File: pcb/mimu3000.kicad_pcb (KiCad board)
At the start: 2 copper layers, 54.9 x 25.9 mm, 13 parts, among them SW1 ONOFF, U1 AQY211EH, U2 ATTINY48U

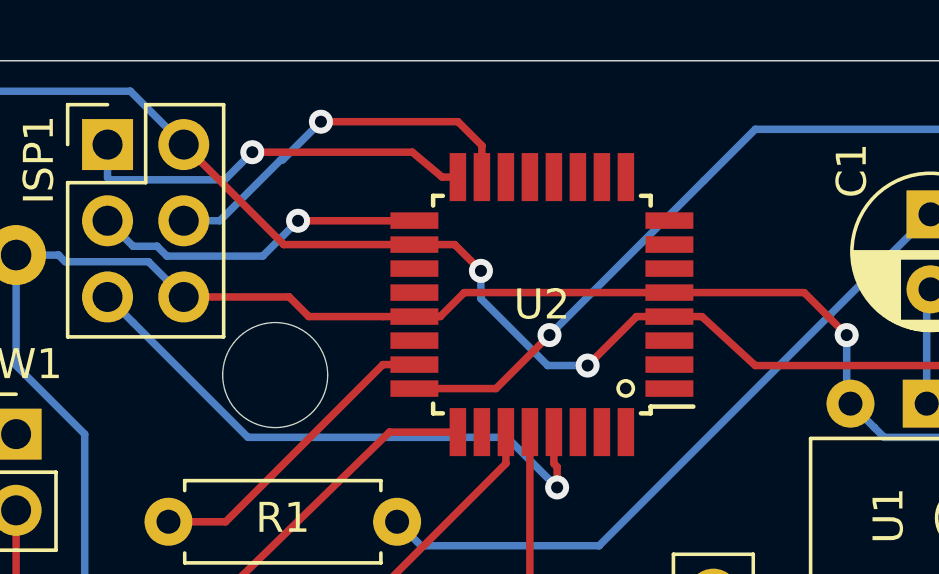
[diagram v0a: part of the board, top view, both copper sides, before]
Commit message: Still too much progmem
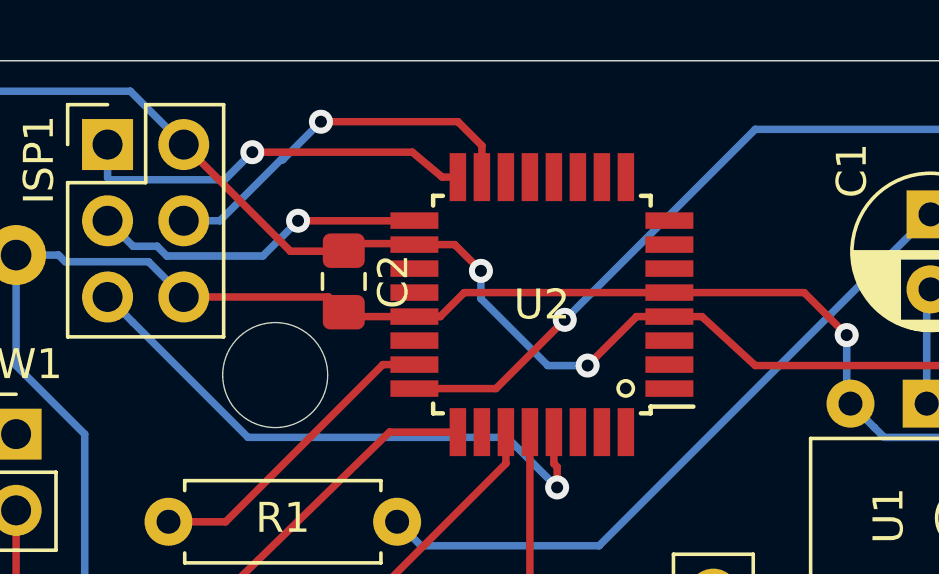
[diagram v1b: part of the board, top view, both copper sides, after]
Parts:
- added C2: 0.1uF, Capacitor_SMD:C_0805_2012Metric_Pad1.15x1.40mm_HandSolder, F.Cu at (178.6, 108.2)
- renumbered BT to BT1
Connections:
- U2 pad 1: Net-(U2-Pad1) -> (no net)
- U2 pad 10: Net-(U2-Pad10) -> (no net)
- U2 pad 11: Net-(U2-Pad11) -> (no net)
- U2 pad 12: Net-(U2-Pad12) -> (no net)
- U2 pad 13: Net-(U2-Pad13) -> (no net)
- U2 pad 14: Net-(U2-Pad14) -> (no net)
- U2 pad 19: Net-(U2-Pad19) -> (no net)
- U2 pad 2: Net-(U2-Pad2) -> (no net)
- U2 pad 20: Net-(U2-Pad20) -> (no net)
- U2 pad 22: Net-(U2-Pad22) -> (no net)
- U2 pad 26: Net-(U2-Pad26) -> (no net)
- U2 pad 3: Net-(U2-Pad3) -> (no net)
- U2 pad 30: Net-(U2-Pad30) -> (no net)
- U2 pad 31: Net-(U2-Pad31) -> (no net)
- U2 pad 32: Net-(U2-Pad32) -> (no net)
- U2 pad 6: Net-(U2-Pad6) -> (no net)
- U2 pad 7: Net-(U2-Pad7) -> (no net)
- U2 pad 8: Net-(U2-Pad8) -> (no net)
- U2 pad 9: Net-(U2-Pad9) -> (no net)

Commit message: We have to use Attiny88
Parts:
- added C3: 0.1uF, Capacitor_SMD:C_0805_2012Metric_Pad1.15x1.40mm_HandSolder, F.Cu at (186.7, 103.4)
- U2: value ATTINY48U -> ATTINY88AU; footprint Housings_QFP:TQFP-32_7x7mm_Pitch0.8mm -> Package_DFN_QFN:QFN-32-1EP_5x5mm_P0.5mm_EP3.1x3.1mm
- moved C2 12.7 mm to (191.3, 108.5), turned to 90 degrees
- moved U2 1.48 mm to (185.9, 107.7)
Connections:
- U2 pad 18: +3V0 -> Net-(C3-Pad1)
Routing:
- net +3V0: track 91.3 -> 102.8 mm
- net Net-(C3-Pad1): track 0.00 -> 9.23 mm, vias 0 -> 2
- net LED: track 12.6 -> 16.5 mm
- net Net-(SENS1-Pad4): track 14.4 -> 17.9 mm
- net Net-(SENS1-Pad3): track 21.6 -> 25.0 mm
- net MUTE: track 10.4 -> 13.4 mm
- net Net-(ISP1-Pad3): track 11.4 -> 13.9 mm
- net GND: track 140.4 -> 138.1 mm
- net Net-(ISP1-Pad1): track 13.5 -> 15.5 mm
- net Net-(ISP1-Pad4): track 13.3 -> 14.7 mm
- net POT: track 38.4 -> 39.6 mm
- net Net-(ISP1-Pad5): track 19.5 -> 20.5 mm

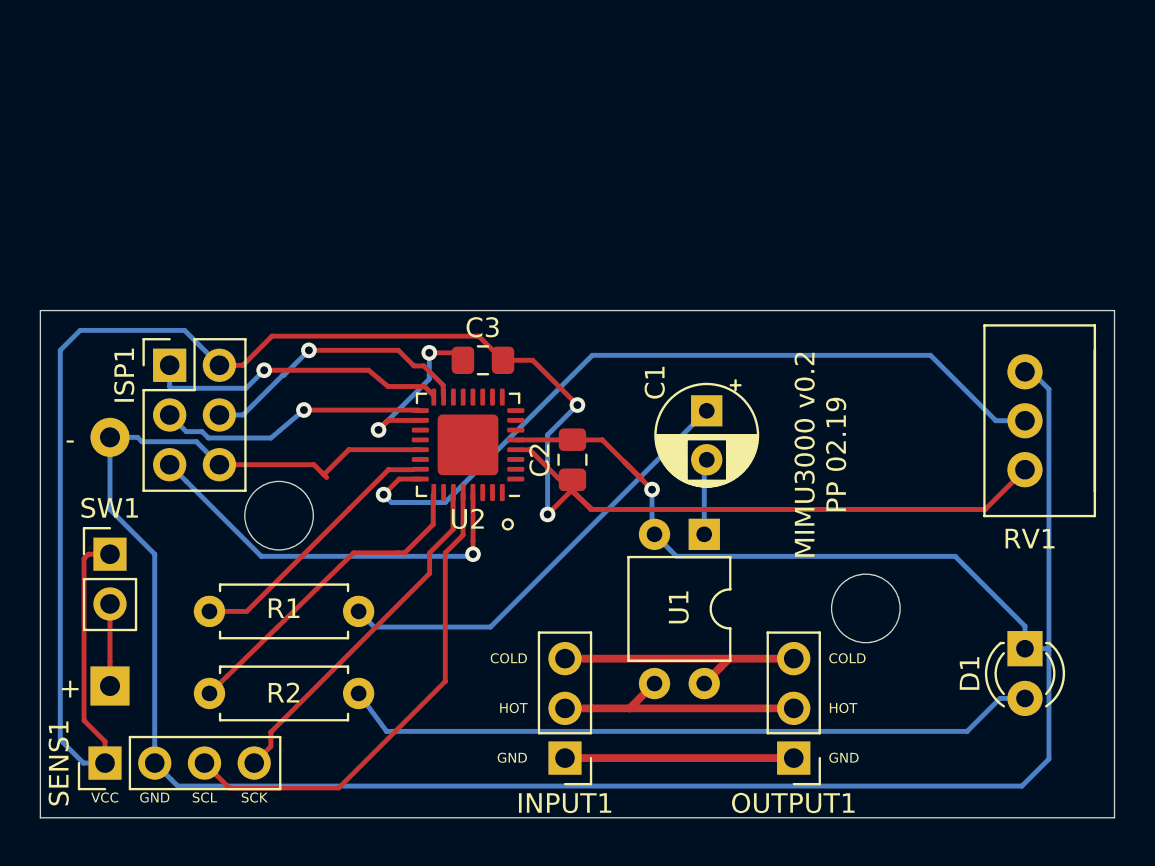
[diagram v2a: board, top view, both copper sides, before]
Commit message: Added 3 extra IO
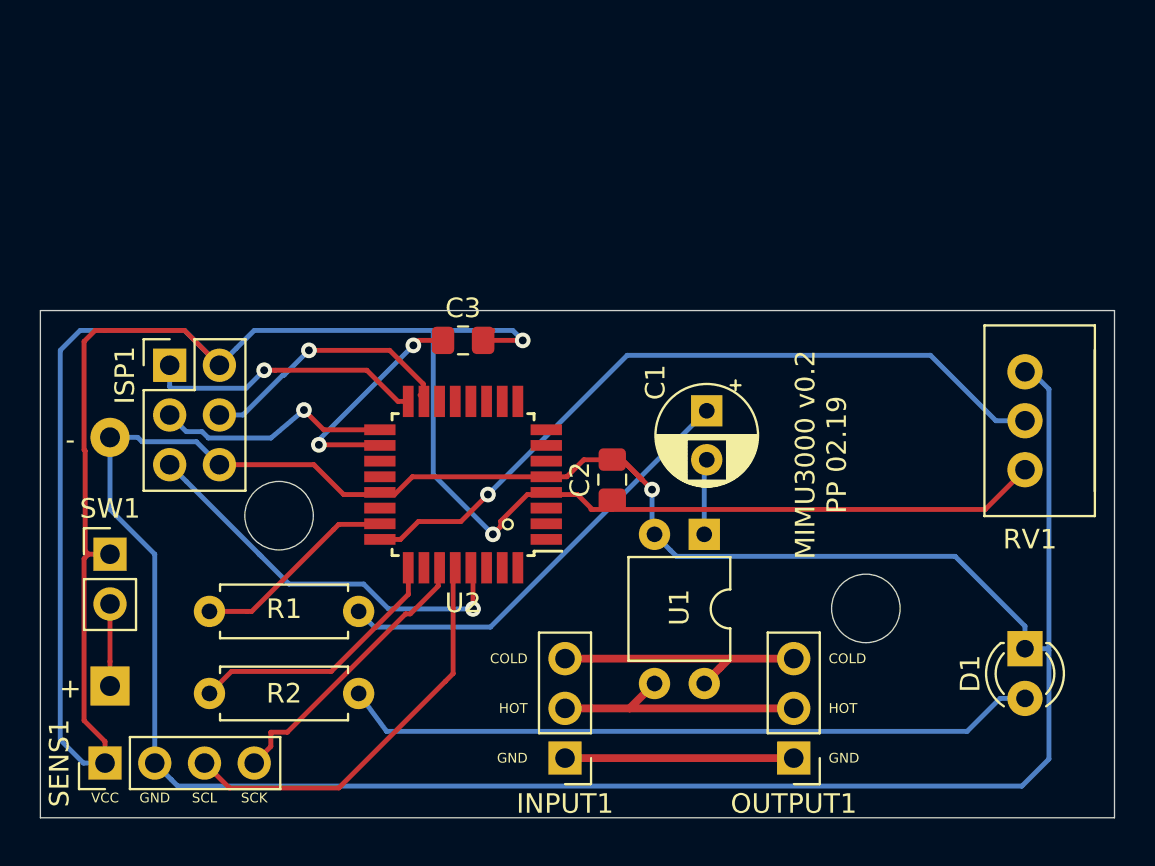
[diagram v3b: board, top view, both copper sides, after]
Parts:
- U2: footprint Package_DFN_QFN:QFN-32-1EP_5x5mm_P0.5mm_EP3.1x3.1mm -> Package_QFP:TQFP-32_7x7mm_P0.8mm
- moved C2 2.27 mm to (193.3, 109.5)
- moved U2 2.05 mm to (185.7, 109.7)
- moved C3 1.44 mm to (185.7, 102.4)
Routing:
- net +3V0: track 102.8 -> 124.1 mm
- net GND: track 138.1 -> 142.7 mm
- net Net-(SENS1-Pad3): track 25.0 -> 21.0 mm
- net Net-(SENS1-Pad4): track 17.9 -> 14.4 mm
- net MUTE: track 13.4 -> 10.2 mm
- net Net-(C3-Pad1): track 9.23 -> 12.3 mm
- net LED: track 16.5 -> 13.5 mm
- net Net-(ISP1-Pad3): track 13.9 -> 12.3 mm
- net POT: track 39.6 -> 38.2 mm
- net Net-(ISP1-Pad1): track 15.5 -> 14.4 mm
- net Net-(ISP1-Pad4): track 14.7 -> 13.9 mm

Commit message: Use realworld-potentiometer
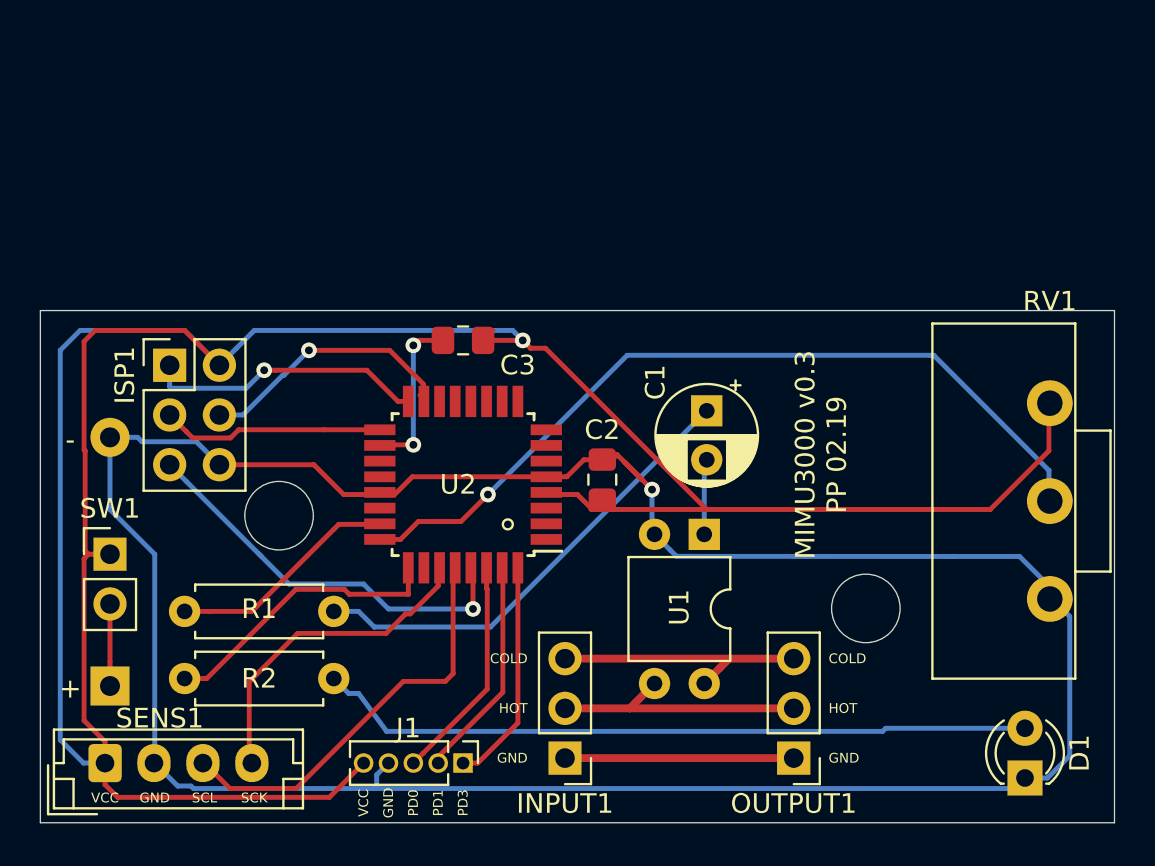
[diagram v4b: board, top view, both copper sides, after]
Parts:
- added J1: OPT, Connector_PinHeader_1.27mm:PinHeader_1x05_P1.27mm_Vertical, F.Cu at (185.7, 124.0)
- BT1: value 3V -> 4.5V
- R1: value 580R -> 110R
- R2: value 90R -> 165R
- RV1: value R_POT -> 1K_POT; footprint Potentiometer_THT:Potentiometer_Alps_RK09Y11_Single_Horizontal -> custom:Potentiometer_Generic_5mm_Single_Horizontal
- SENS1: footprint Connector_PinHeader_2.54mm:PinHeader_1x04_P2.54mm_Vertical -> Connector_JST:JST_EH_B4B-EH-A_1x04_P2.50mm_Vertical
- moved RV1 6.73 mm to (215.6, 115.6)
- moved D1 6.60 mm to (214.4, 124.7), turned to 90 degrees
- moved R2 1.48 mm to (171.4, 119.6)
- moved R1 1.27 mm to (171.4, 116.2)
- moved C2 0.51 mm to (192.8, 109.5)
- turned SENS1 to 0 degrees
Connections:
- RV1 pad 1: +3V0 -> GND
- RV1 pad 3: GND -> +3V0
- U2 pad 30: (no net) -> Net-(J1-Pad3)
- U2 pad 31: (no net) -> Net-(J1-Pad2)
- U2 pad 32: (no net) -> Net-(J1-Pad1)
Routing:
- net +3V0: track 124.1 -> 140.9 mm, vias 2 -> 1
- net Net-(J1-Pad1): track 0.00 -> 11.6 mm
- net Net-(J1-Pad3): track 0.00 -> 11.6 mm
- net Net-(J1-Pad2): track 0.00 -> 11.0 mm
- net GND: track 142.7 -> 132.6 mm
- net Net-(C3-Pad1): track 12.3 -> 8.48 mm
- net POT: track 38.2 -> 42.0 mm
- net Net-(SENS1-Pad4): track 14.4 -> 16.7 mm
- net Net-(C1-Pad1): track 22.7 -> 24.0 mm
- net MUTE: track 10.2 -> 11.4 mm
- net LED: track 13.5 -> 14.4 mm
- net Net-(ISP1-Pad3): track 12.3 -> 11.6 mm, vias 1 -> 0
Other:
- board size 54.9 x 25.9 mm -> 54.9 x 26.2 mm
- board text added: "MIMU3000 v0.3 PP 02.19"
- board text added: "PD0"
- board text added: "PD1"
- board text added: "PD3"
- board text removed: "MIMU3000 v0.2 PP 02.19"

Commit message: Switched to 3xAAA container, Vertically fixed Sensor and the possibility to adding a tantal for de-pop
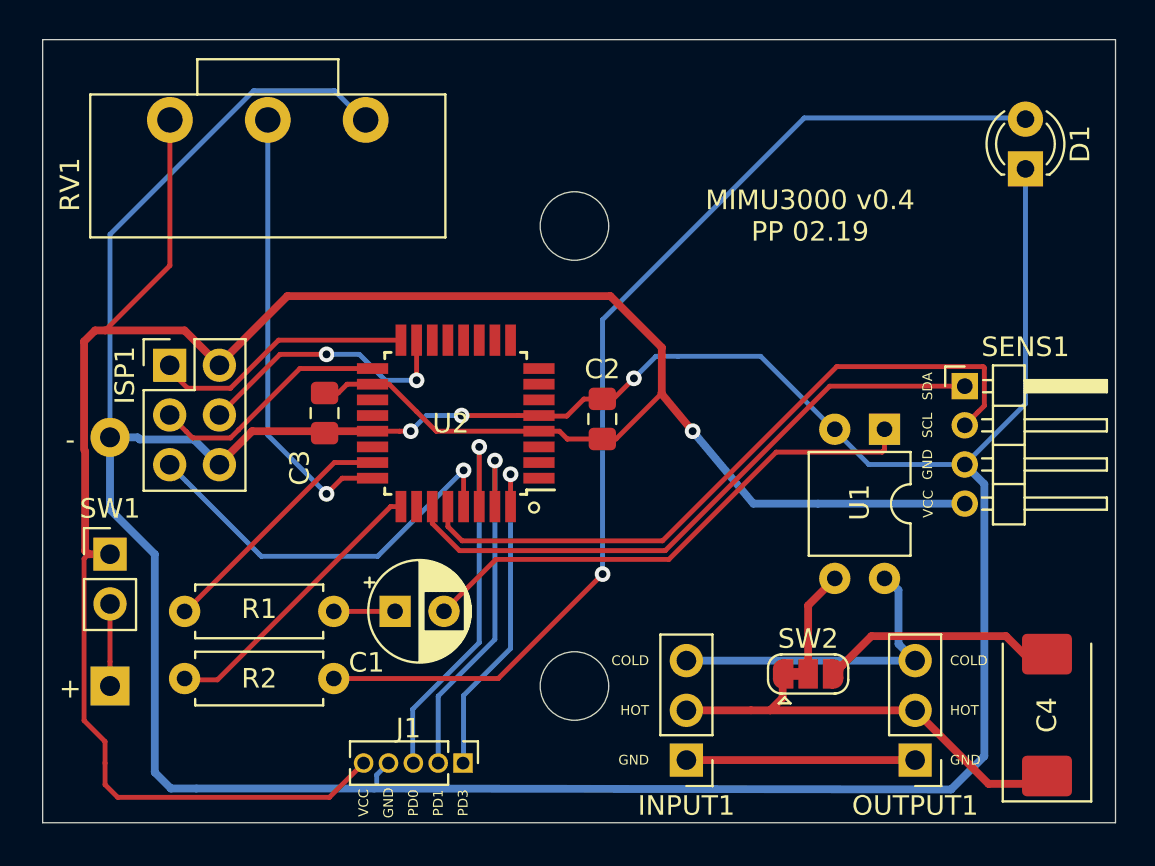
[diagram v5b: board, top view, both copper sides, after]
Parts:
- added C4: 1000uF, Capacitor_Tantalum_SMD:CP_EIA-7343-15_Kemet-W, F.Cu at (215.5, 121.5)
- added SW2: SW_DPDT_x2, Jumper:SolderJumper-3_P1.3mm_Bridged12_RoundedPad1.0x1.5mm, F.Cu at (203.3, 119.4)
- BT1: footprint Battery_Holders:Keystone_2468_2xAAA -> custom:BatteryHolder_Generic_3xAAA
- SENS1: footprint Connector_JST:JST_EH_B4B-EH-A_1x04_P2.50mm_Vertical -> Connector_PinHeader_2.00mm:PinHeader_1x04_P2.00mm_Horizontal
- moved SENS1 47.9 mm to (211.3, 104.7)
- moved RV1 42.7 mm to (180.7, 91.1), turned to 90 degrees
- moved D1 31.1 mm to (214.4, 93.6)
- moved C1 18.9 mm to (182.2, 116.2), turned to 0 degrees
- moved U1 10.7 mm to (207.2, 106.9)
- moved C3 7.99 mm to (178.6, 106.1), turned to 270 degrees
- moved INPUT1 6.20 mm to (197.1, 123.8)
- moved OUTPUT1 6.20 mm to (208.8, 123.8)
- moved U2 3.15 mm to (185.3, 106.6)
- moved C2 3.10 mm to (192.8, 106.4)
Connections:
- C3 pad 1: Net-(C3-Pad1) -> +3V0
- C3 pad 2: +3V0 -> GND
- INPUT1 pad 2: Net-(INPUT1-Pad2) -> Net-(C4-Pad1)
- OUTPUT1 pad 2: Net-(INPUT1-Pad2) -> Net-(C4-Pad1)
- SENS1 pad 1: +3V0 -> SDA
- SENS1 pad 2: GND -> SCL
- SENS1 pad 3: Net-(SENS1-Pad3) -> GND
- SENS1 pad 4: Net-(SENS1-Pad4) -> +3V0
- U1 pad 3: Net-(INPUT1-Pad2) -> Net-(SW2-Pad2)
- U2 pad 18: Net-(C3-Pad1) -> +3V0
- U2 pad 27: Net-(SENS1-Pad4) -> SDA
- U2 pad 28: Net-(SENS1-Pad3) -> SCL
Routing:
- net GND: track 132.6 -> 171.4 mm, vias 1 -> 3
- net SCL: track 0.00 -> 35.8 mm
- net SDA: track 0.00 -> 32.0 mm
- net Net-(C1-Pad2): track 3.86 -> 27.0 mm
- net Net-(C4-Pad1): track 0.00 -> 22.5 mm
- net Net-(SENS1-Pad3): track 21.0 -> 0.00 mm
- net Net-(C1-Pad1): track 24.0 -> 3.12 mm
- net POT: track 42.0 -> 23.0 mm
- net Net-(D1-Pad2): track 36.7 -> 54.9 mm, vias 0 -> 1
- net +3V0: track 140.9 -> 123.7 mm
- net Net-(SENS1-Pad4): track 16.7 -> 0.00 mm
- net Net-(INPUT1-Pad2): track 13.5 -> 0.00 mm
- net Net-(C4-Pad2): track 0.00 -> 12.8 mm
- net Net-(J1-Pad3): track 11.6 -> 20.7 mm, vias 0 -> 1
- net Net-(C3-Pad1): track 8.48 -> 0.00 mm, vias 2 -> 0
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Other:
- board size 54.9 x 26.2 mm -> 54.8 x 40 mm
- board text added: "MIMU3000 v0.4 PP 02.19"
- board text added: "SDA"
- board text added: "lol"
- board text removed: "MIMU3000 v0.3 PP 02.19"
- board text removed: "SCK"

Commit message: added JCL number placeholder
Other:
- board text added: "JLCJLCJLCJLC"
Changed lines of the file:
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@@
   (general
     (thickness 1.6)
-    (drawings 34)
+    (drawings 35)
     (tracks 190)
     (zones 0)
@@
     (descr "3xAAA cell battery holder, Keystone P/N 2479, http://www.keyelco.com/product-pdf.cfm?p=1041")
     (tags "AAA battery cell holder")
-    (fp_text reference BT1 (at 0 7 -180) (layer B.SilkS)
+    (fp_text reference BT1 (at 0 2.785 -180) (layer B.SilkS)
       (effects (font (size 1 1) (thickness 0.15)) (justify mirror))
     )
@@
       (effects (font (size 1 1) (thickness 0.15)) (justify mirror))
     )
-    (fp_text user + (at -3.81 0) (layer B.SilkS)
+    (fp_text user + (at -2.04 0.085) (layer B.SilkS)
       (effects (font (size 1.5 1.5) (thickness 0.15)) (justify mirror))
     )
-    (fp_text user - (at -3.81 -12.7) (layer B.SilkS)
+    (fp_text user - (at -2.14 -12.615) (layer B.SilkS)
       (effects (font (size 1.5 1.5) (thickness 0.15)) (justify mirror))
     )
@@
     )
   )
-  (gr_text lol (at 169.3 95.7 90) (layer B.SilkS)
+  (gr_text JLCJLCJLCJLC (at 172.4 99.4 180) (layer B.SilkS)
     (effects (font (size 1 1) (thickness 0.15)) (justify mirror))
   )
+  (gr_text lol (at 172.4 100.9) (layer B.SilkS)
+    (effects (font (size 1 1) (thickness 0.15)) (justify mirror))
+  )
